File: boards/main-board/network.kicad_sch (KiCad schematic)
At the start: 24 parts, among them J3 RJ45_Bel_SI-60062-F, J6 DNF, U4 ESP32-WROOM-32D, U5 LAN8720A, Y2 25MHz

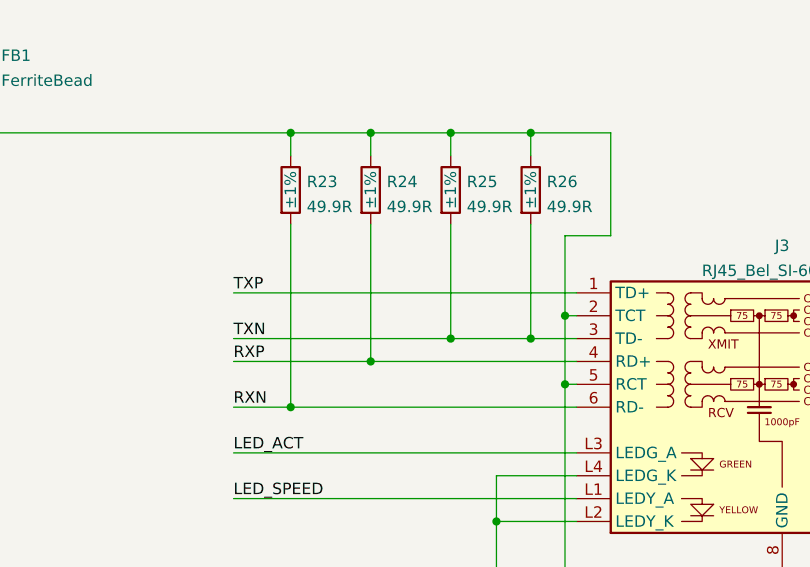
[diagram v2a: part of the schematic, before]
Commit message: Fixed resistor connecting to wrong line
Signed-off-by: Computroniks <mnickson@sidingsmedia.com>
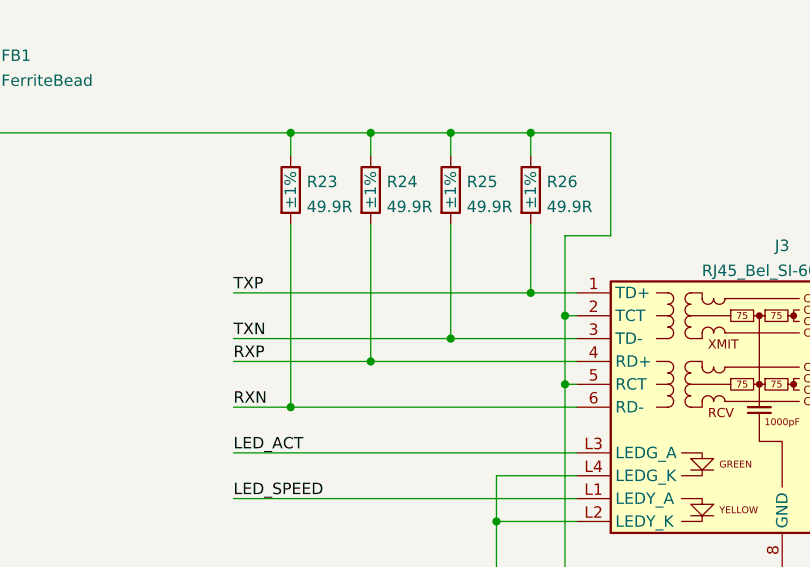
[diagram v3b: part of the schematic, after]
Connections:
- net TXN: no longer R26.2
- net TXP: now also R26.2
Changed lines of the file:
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@@
   (junction (at 219.71 55.88) (diameter 0) (color 0 0 0 0)
   )
-  (junction (at 228.6 55.88) (diameter 0) (color 0 0 0 0)
-  )
   (junction (at 201.93 63.5) (diameter 0) (color 0 0 0 0)
   )
@@
   )
   (junction (at 118.11 97.79) (diameter 0) (color 0 0 0 0)
+  )
+  (junction (at 228.6 50.8) (diameter 0) (color 0 0 0 0)
   )
   (junction (at 105.41 156.21) (diameter 0) (color 0 0 0 0)
@@
     (stroke (width 0) (type default) (color 0 0 0 0))
   )
+  (wire (pts (xy 228.6 43.18) (xy 228.6 50.8))
+    (stroke (width 0) (type default) (color 0 0 0 0))
+  )
   (wire (pts (xy 21.59 41.91) (xy 21.59 44.45))
     (stroke (width 0) (type default) (color 0 0 0 0))
@@
     (stroke (width 0) (type default) (color 0 0 0 0))
   )
-  (wire (pts (xy 228.6 55.88) (xy 233.68 55.88))
-    (stroke (width 0) (type default) (color 0 0 0 0))
-  )
   (wire (pts (xy 128.27 144.78) (xy 139.7 144.78))
     (stroke (width 0) (type default) (color 0 0 0 0))
@@
     (stroke (width 0) (type default) (color 0 0 0 0))
   )
-  (wire (pts (xy 195.58 50.8) (xy 233.68 50.8))
+  (wire (pts (xy 195.58 50.8) (xy 228.6 50.8))
     (stroke (width 0) (type default) (color 0 0 0 0))
   )
@@
     (stroke (width 0) (type default) (color 0 0 0 0))
   )
+  (wire (pts (xy 228.6 50.8) (xy 233.68 50.8))
+    (stroke (width 0) (type default) (color 0 0 0 0))
+  )
   (wire (pts (xy 68.58 35.56) (xy 83.82 35.56))
     (stroke (width 0) (type default) (color 0 0 0 0))
@@
     (stroke (width 0) (type default) (color 0 0 0 0))
   )
-  (wire (pts (xy 228.6 43.18) (xy 228.6 55.88))
-    (stroke (width 0) (type default) (color 0 0 0 0))
-  )
   (wire (pts (xy 118.11 96.52) (xy 118.11 97.79))
     (stroke (width 0) (type default) (color 0 0 0 0))
@@
     (stroke (width 0) (type default) (color 0 0 0 0))
   )
-  (wire (pts (xy 219.71 55.88) (xy 228.6 55.88))
-    (stroke (width 0) (type default) (color 0 0 0 0))
-  )
+  (wire (pts (xy 219.71 55.88) (xy 233.68 55.88))
+    (stroke (width 0) (type default) (color 0 0 0 0))
+  )

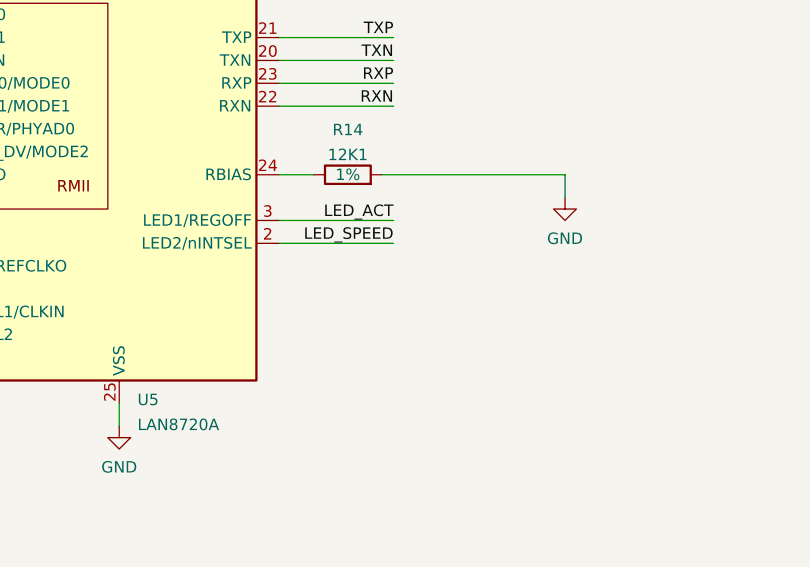
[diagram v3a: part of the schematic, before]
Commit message: Added resistors for LEDs
Signed-off-by: Computroniks <mnickson@sidingsmedia.com>
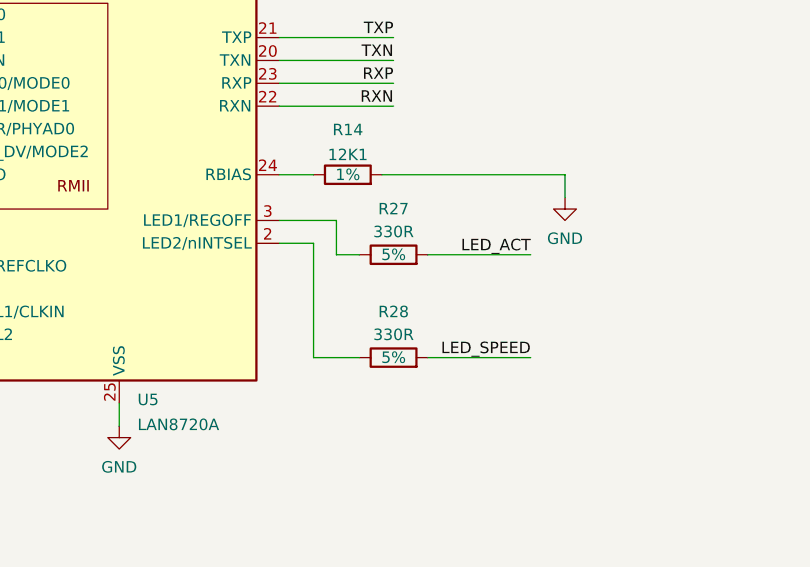
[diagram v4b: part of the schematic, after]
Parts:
- added R27, R28: 330R, Resistor_SMD:R_0805_2012Metric, symbol Device:R
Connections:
- net LED_ACT: now also R27.2; no longer U5.3 (LED1/REGOFF)
- net LED_SPEED: now also R28.2; no longer U5.2 (LED2/nINTSEL)
- new net: R28.1, U5.2 (LED2/nINTSEL)
- new net: R27.1, U5.3 (LED1/REGOFF)
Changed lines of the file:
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@@
+    (stroke (width 0) (type default) (color 0 0 0 0))
+  )
+  (wire (pts (xy 177.8 147.32) (xy 184.15 147.32))
     (stroke (width 0) (type default) (color 0 0 0 0))
   )
@@
     (stroke (width 0) (type default) (color 0 0 0 0))
   )
+  (wire (pts (xy 194.31 151.13) (xy 205.74 151.13))
+    (stroke (width 0) (type default) (color 0 0 0 0))
+  )
   (wire (pts (xy 135.89 160.02) (xy 135.89 172.72))
     (stroke (width 0) (type default) (color 0 0 0 0))
@@
     (stroke (width 0) (type default) (color 0 0 0 0))
   )
+  (wire (pts (xy 194.31 162.56) (xy 205.74 162.56))
+    (stroke (width 0) (type default) (color 0 0 0 0))
+  )
   (wire (pts (xy 128.27 144.78) (xy 139.7 144.78))
     (stroke (width 0) (type default) (color 0 0 0 0))
@@
     (stroke (width 0) (type default) (color 0 0 0 0))
   )
-  (wire (pts (xy 177.8 149.86) (xy 190.5 149.86))
-    (stroke (width 0) (type default) (color 0 0 0 0))
-  )
   (wire (pts (xy 68.58 76.2) (xy 83.82 76.2))
     (stroke (width 0) (type default) (color 0 0 0 0))
@@
     (stroke (width 0) (type default) (color 0 0 0 0))
   )
+  (wire (pts (xy 184.15 151.13) (xy 186.69 151.13))
+    (stroke (width 0) (type default) (color 0 0 0 0))
+  )
+  (wire (pts (xy 181.61 149.86) (xy 177.8 149.86))
+    (stroke (width 0) (type default) (color 0 0 0 0))
+  )
   (wire (pts (xy 68.58 53.34) (xy 78.74 53.34))
     (stroke (width 0) (type default) (color 0 0 0 0))
@@
     (stroke (width 0) (type default) (color 0 0 0 0))
   )
+  (wire (pts (xy 181.61 149.86) (xy 181.61 162.56))
+    (stroke (width 0) (type default) (color 0 0 0 0))
+  )
   (wire (pts (xy 118.11 137.16) (xy 139.7 137.16))
     (stroke (width 0) (type default) (color 0 0 0 0))
@@
     (stroke (width 0) (type default) (color 0 0 0 0))
   )
+  (wire (pts (xy 184.15 147.32) (xy 184.15 151.13))
+    (stroke (width 0) (type default) (color 0 0 0 0))
+  )
   (wire (pts (xy 115.57 53.34) (xy 115.57 50.8))
     (stroke (width 0) (type default) (color 0 0 0 0))
@@
     (stroke (width 0) (type default) (color 0 0 0 0))
   )
-  (wire (pts (xy 177.8 147.32) (xy 190.5 147.32))
-    (stroke (width 0) (type default) (color 0 0 0 0))
-  )
   (wire (pts (xy 123.19 185.42) (xy 123.19 187.96))
     (stroke (width 0) (type default) (color 0 0 0 0))
@@
     (stroke (width 0) (type default) (color 0 0 0 0))
   )
+  (wire (pts (xy 181.61 162.56) (xy 186.69 162.56))
+    (stroke (width 0) (type default) (color 0 0 0 0))
+  )
   (wire (pts (xy 219.71 55.88) (xy 233.68 55.88))
     (stroke (width 0) (type default) (color 0 0 0 0))
@@
     (effects (font (size 1.27 1.27)) (justify left bottom))
   )
-  (label "LED_ACT" (at 190.5 147.32 180)
+  (label "LED_ACT" (at 205.74 151.13 180)
     (effects (font (size 1.27 1.27)) (justify right bottom))
   )
@@
     (effects (font (size 1.27 1.27)) (justify right bottom))
   )
-  (label "LED_SPEED" (at 190.5 149.86 180)
+  (label "LED_SPEED" (at 205.74 162.56 180)
     (effects (font (size 1.27 1.27)) (justify right bottom))
   )
@@
     (pin "2")
   )
+  (symbol (lib_id "Device:R") (at 190.5 151.13 90) (unit 1)
+    (in_bom yes) (on_board yes)
+    (property "Reference" "R27" (id 0) (at 190.5 146.05 90))
+    (property "Value" "330R" (id 1) (at 190.5 148.59 90))
+    (property "Footprint" "Resistor_SMD:R_0805_2012Metric" (id 2) (at 190.5 152.908 90)
+      (effects (font (size 1.27 1.27)) hide)
+    )
+    (property "Datasheet" "~" (id 3) (at 190.5 151.13 0)
+      (effects (font (size 1.27 1.27)) hide)
+    )
+    (property "Tolerance" "5%" (id 4) (at 190.5 151.13 90))
+    (pin "1")
+    (pin "2")
+  )
   (symbol (lib_id "Device:C_Polarized") (at 21.59 38.1 0) (unit 1)
     (in_bom yes) (on_board yes) (fields_autoplaced)
@@
     (pin "1")
     (pin "2")
+  )
+  (symbol (lib_id "Device:R") (at 190.5 162.56 90) (unit 1)
+    (in_bom yes) (on_board yes)
+    (property "Reference" "R28" (id 0) (at 190.5 157.48 90))
+    (property "Value" "330R" (id 1) (at 190.5 160.02 90))
+    (property "Footprint" "Resistor_SMD:R_0805_2012Metric" (id 2) (at 190.5 164.338 90)
+      (effects (font (size 1.27 1.27)) hide)
+    )
+    (property "Datasheet" "~" (id 3) (at 190.5 162.56 0)
+      (effects (font (size 1.27 1.27)) hide)
+    )
+    (property "Tolerance" "5%" (id 4) (at 190.5 162.56 90))
+    (pin "1")
+    (pin "2")
